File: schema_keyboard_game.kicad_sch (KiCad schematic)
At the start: 229 parts, among them J1 USB_C_Receptacle_PowerOnly_6P, J2 Conn_01x04, SW101 SW_Push, U1 ESP32-S3-DevKitC

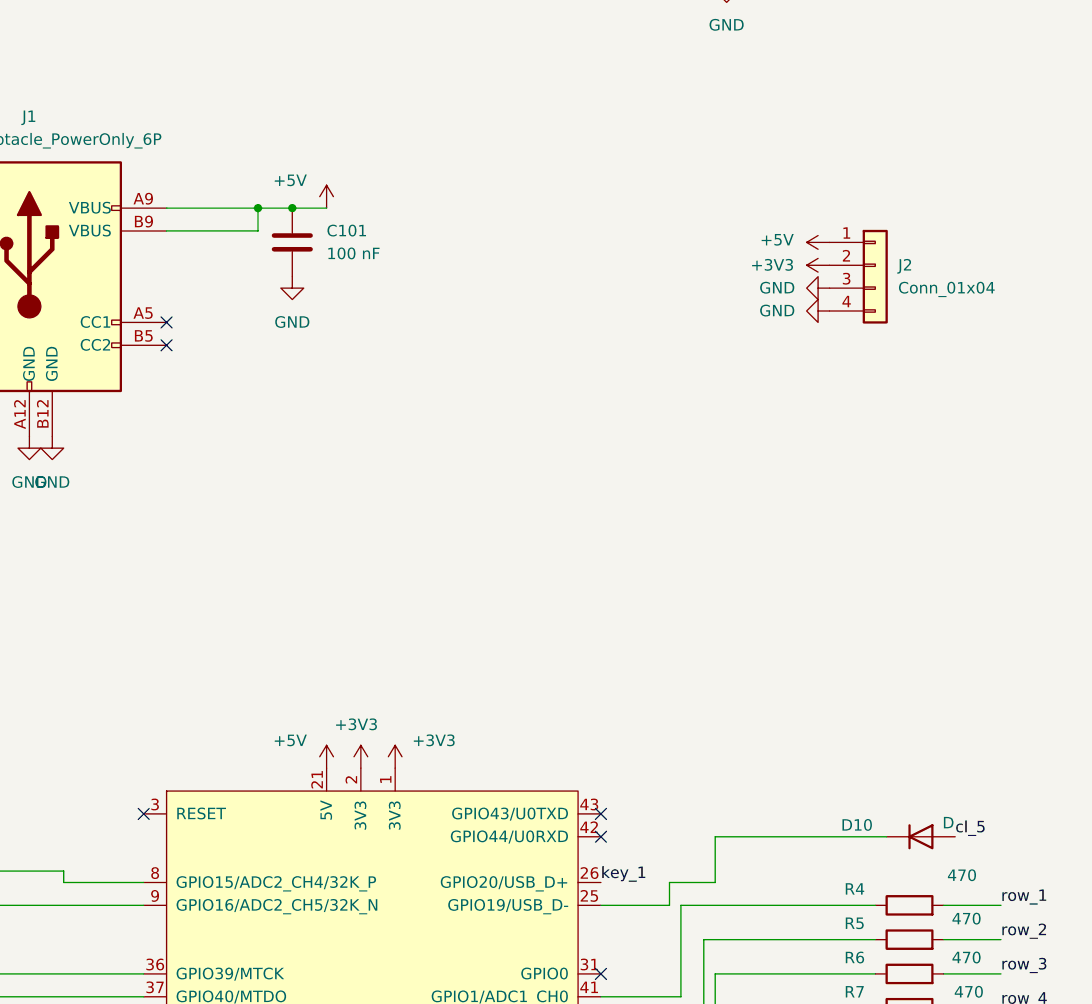
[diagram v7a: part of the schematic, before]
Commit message: Update schema with new out pins
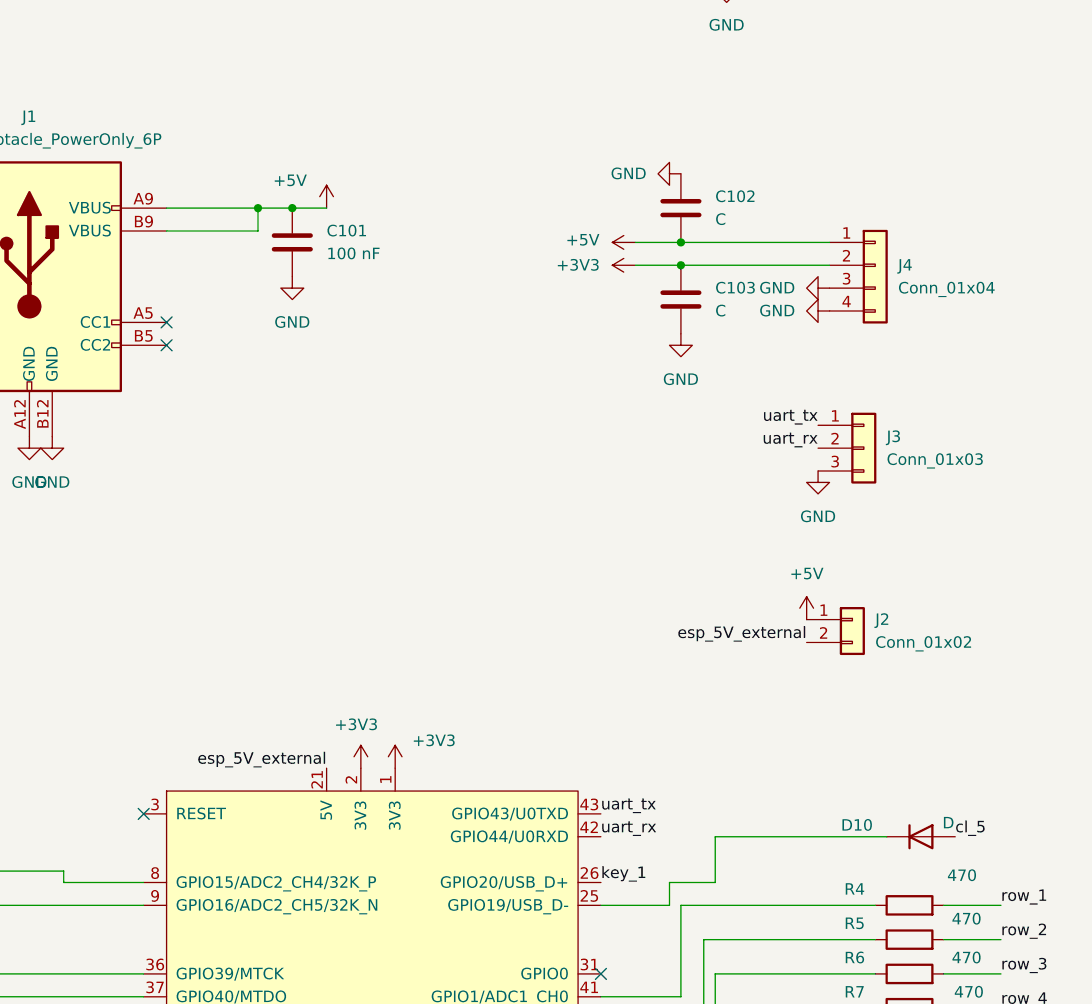
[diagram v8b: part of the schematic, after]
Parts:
- added C102, C103: C, Capacitor_SMD:C_1206_3216Metric, symbol Device:C
- added J2: Conn_01x02, Connector_PinHeader_2.54mm:PinHeader_1x02_P2.54mm_Vertical, symbol Connector_Generic:Conn_01x02
- added J3: Conn_01x03, Connector_PinHeader_2.54mm:PinHeader_1x03_P2.54mm_Vertical, symbol Connector_Generic:Conn_01x03
- renumbered J2 to J4
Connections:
- net +3V3: now also C103.1
- net +5V: now also C102.2, J2.1 (Pin_1); no longer U1.21 (5V)
- net GND: now also C102.1, C103.2, J3.3 (Pin_3)
- net uart_rx: now reaches U1.42 (GPIO44/U0RXD)
- net uart_rx: now also J3.2 (Pin_2)
- net uart_tx: now reaches U1.43 (GPIO43/U0TXD)
- net uart_tx: now also J3.1 (Pin_1)
- new net esp_5V_external: J2.2 (Pin_2), U1.21 (5V)
- no-connect marks 14 -> 12
